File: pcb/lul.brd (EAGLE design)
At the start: 90 x 96 mm, 85 parts, among them IC1 STM32F072C8T6, IC2 REG1117, IC3 74AHCT1G08DBV, SW1 324_SW324_SWITCH_FOOT_HOLE, SW2 324_SW324_SWITCH_FOOT_HOLE, SW3 324_SW324_SWITCH_FOOT_HOLE, SW4 324_SW324_SWITCH_FOOT_HOLE, U1 UG-2864HSWEG01, U2 USBC_16P

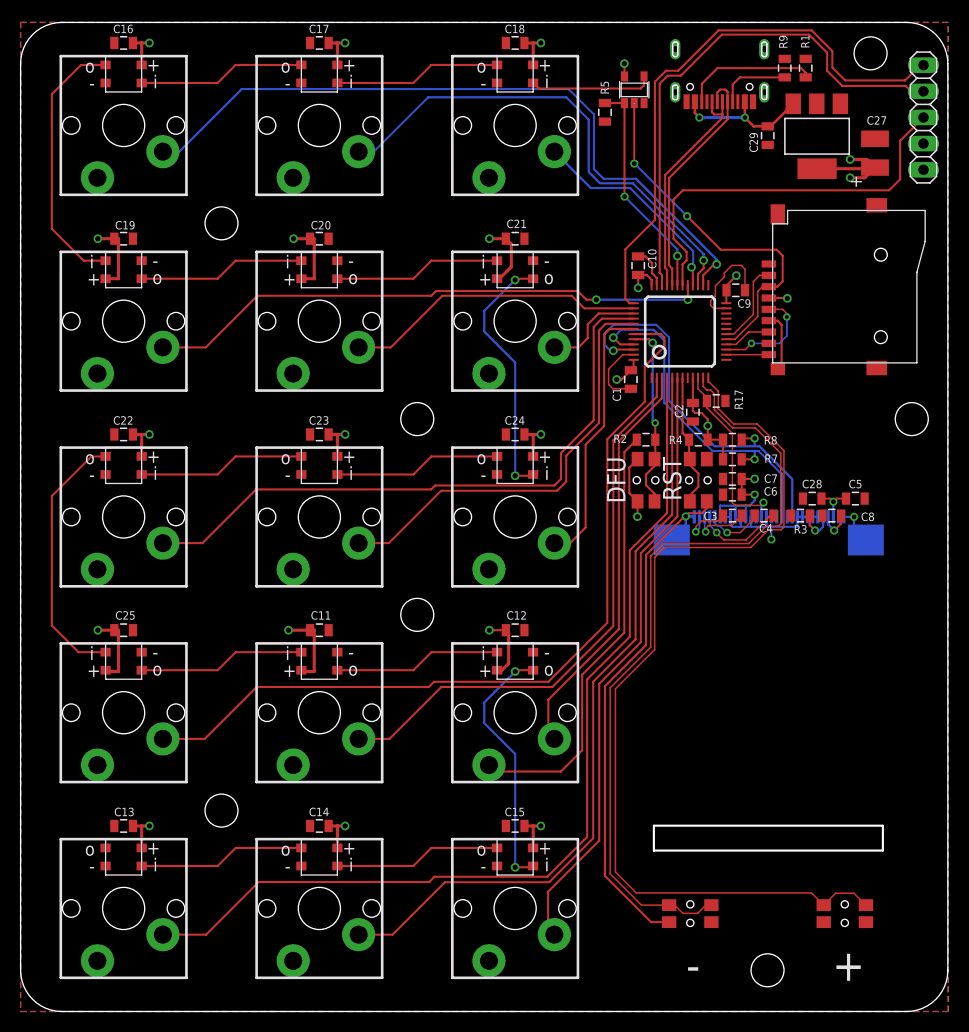
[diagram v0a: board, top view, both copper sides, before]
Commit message: simpler version for jlcpcb assembly
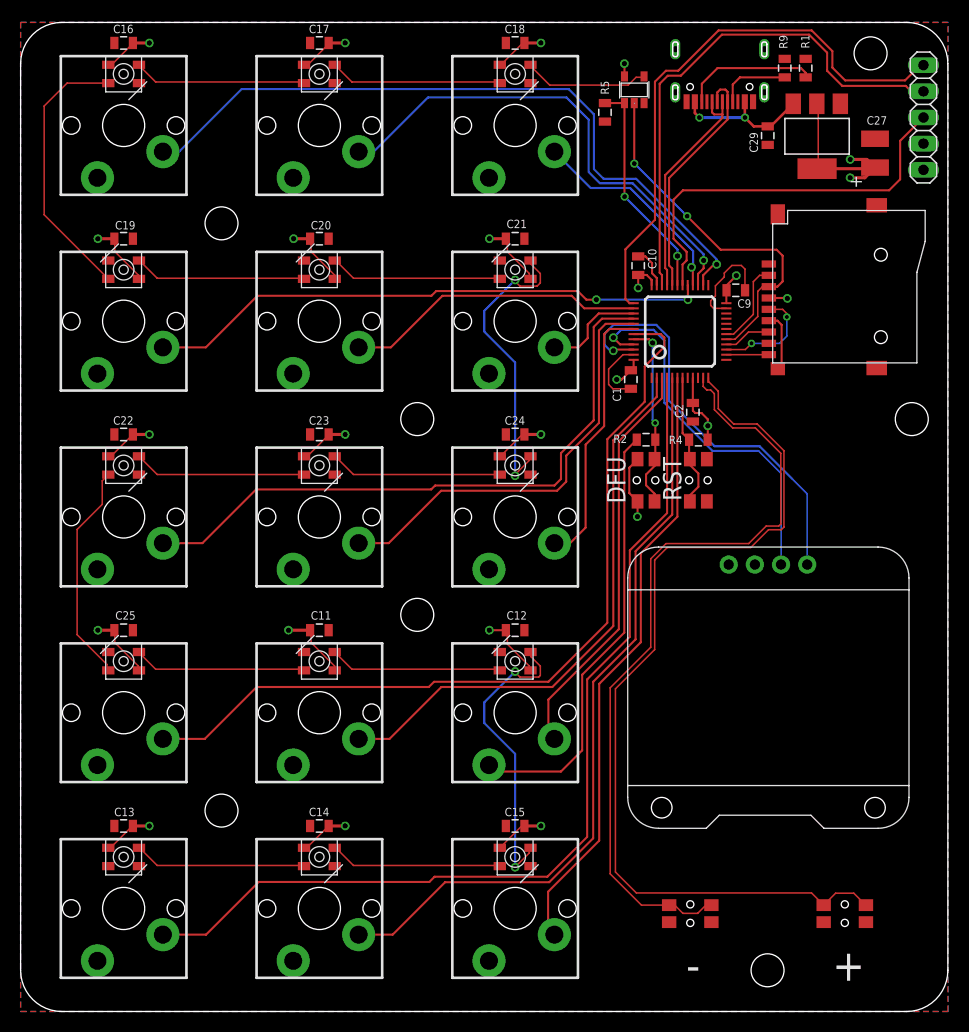
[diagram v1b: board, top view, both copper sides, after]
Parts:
- removed C28, C3, C4, C6: 1uF, clock:0805@1
- removed C5, C7, C8: 2.2uF, clock:0805@1
- removed R17: 10K, clock:0805
- removed R3: 560K, clock:0805
- removed R7, R8: 5.1K, clock:0805
- removed U1: UG-2864HSWEG01, lul:LUL_UG-2864HSWEG01_1.3_WRAPAROUND
- added U$2: OLED_0.96_I2C, tft_1.8_1.44_oled_0.96:OLED_0.96_I2C
- LED1, LED10, LED11, LED12, LED13, LED14, LED15, LED2, LED3, LED4, LED5, LED6, LED7, LED8, LED9: value WS2812B3535 -> WS2812B-MINI; device lul:LED3535 -> LED:WS2812B-MINI
- turned LED1 to 90 degrees
- turned LED10 to 270 degrees
- turned LED11 to 270 degrees
- turned LED12 to 270 degrees
- turned LED13 to 90 degrees
- turned LED14 to 90 degrees
- turned LED15 to 90 degrees
- turned LED2 to 90 degrees
- turned LED3 to 90 degrees
- turned LED4 to 270 degrees
- turned LED5 to 270 degrees
- turned LED6 to 270 degrees
- turned LED7 to 90 degrees
- turned LED8 to 90 degrees
- turned LED9 to 90 degrees
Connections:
- removed net N$11: C28.2, C5.2, U1.28
- removed net N$12: C8.2, U1.27
- removed net N$3: R3.2, U1.26
- removed net N$4: C3.2, U1.2
- removed net N$5: C3.1, U1.3
- removed net N$6: C4.2, U1.4
- removed net N$7: C4.1, U1.5
- net +3V3: now also LED1.VDD, LED10.VDD, LED11.VDD, LED12.VDD, LED13.VDD, LED14.VDD, LED15.VDD, LED2.VDD, LED3.VDD, LED4.VDD, LED5.VDD, LED6.VDD, LED7.VDD, LED8.VDD, LED9.VDD, U$2.VCC; no longer C6.2, C7.2, LED1.2, LED10.2, LED11.2, LED12.2, LED13.2, LED14.2, LED15.2, LED2.2, LED3.2, LED4.2, LED5.2, LED6.2, LED7.2, LED8.2, LED9.2, R7.2, R8.2, U1.11, U1.6, U1.9
- net GND: now also LED1.GND, LED10.GND, LED11.GND, LED12.GND, LED13.GND, LED14.GND, LED15.GND, LED2.GND, LED3.GND, LED4.GND, LED5.GND, LED6.GND, LED7.GND, LED8.GND, LED9.GND, U$2.GND; no longer C28.1, C5.1, C6.1, C7.1, C8.1, LED1.4, LED10.4, LED11.4, LED12.4, LED13.4, LED14.4, LED15.4, LED2.4, LED3.4, LED4.4, LED5.4, LED6.4, LED7.4, LED8.4, LED9.4, R17.1, R3.1, U1.1, U1.10, U1.12, U1.13, U1.15, U1.16, U1.17, U1.21, U1.22, U1.23, U1.24, U1.25, U1.29, U1.30, U1.31, U1.32, U1.7, U1.8
- net N$15: now also LED1.DI, LED2.DO; no longer LED1.1, LED2.3
- net N$17: now also LED1.DO, LED4.DI; no longer LED1.3, LED4.1
- net N$18: now also LED4.DO, LED5.DI; no longer LED4.3, LED5.1
- net N$19: now also LED5.DO, LED6.DI; no longer LED5.3, LED6.1
- net N$20: now also LED6.DO, LED9.DI; no longer LED6.3, LED9.1
- net N$21: now also LED8.DI, LED9.DO; no longer LED8.1, LED9.3
- net N$22: now also LED7.DI, LED8.DO; no longer LED7.1, LED8.3
- net N$23: now also LED10.DI, LED7.DO; no longer LED10.1, LED7.3
- net N$24: now also LED10.DO, LED11.DI; no longer LED10.3, LED11.1
- net N$25: now also LED11.DO, LED12.DI; no longer LED11.3, LED12.1
- net N$26: now also LED12.DO, LED15.DI; no longer LED12.3, LED15.1
- net N$27: now also LED14.DI, LED15.DO; no longer LED14.1, LED15.3
- net N$28: now also LED13.DI, LED14.DO; no longer LED13.1, LED14.3
- net N$29: now also LED3.DI; no longer LED3.1
- net N$9: now also LED2.DI, LED3.DO; no longer LED2.1, LED3.3
- net OLED_RESET: no longer R17.2, U1.14
- net SCL: now also U$2.SCL; no longer R7.1, U1.18
- net SDA: now also U$2.SDA; no longer R8.1, U1.19, U1.20
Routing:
- net GND: track 142.6 -> 69.3 mm, vias 3 -> 0
- net OLED_RESET: track 18.2 -> 0.00 mm, vias 1 -> 0
- net N$6: track 8.59 -> 0.00 mm, vias 1 -> 0
- net N$5: track 5.84 -> 0.00 mm, vias 1 -> 0
- net N$7: track 5.70 -> 0.00 mm, vias 1 -> 0
- net N$4: track 5.19 -> 0.00 mm, vias 1 -> 0
- net N$26: track 25.1 -> 29.5 mm
- net N$20: track 25.1 -> 29.5 mm
- net N$23: track 25.7 -> 21.5 mm
- net N$11: track 4.12 -> 0.00 mm, vias 1 -> 0
- net N$3: track 3.55 -> 0.00 mm, vias 1 -> 0
- net N$12: track 3.28 -> 0.00 mm, vias 1 -> 0
- net SDA: track 38.8 -> 41.5 mm, vias 2 -> 1
- net SCL: track 34.5 -> 37.0 mm, vias 2 -> 1
- net +3V3: track 127.3 -> 126.7 mm, vias 26 -> 24
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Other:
- outline, holes or cut-outs redrawn
- board text added: "dekuNukem PD1 JUN19 kowmod1"
- board text added: "git.io/kbord"
- board text added: "kbord"
- board text removed: "dekuNukem PD1 JUN19"
- board text removed: "duckypad"
- board text removed: "git.io/duckypad"
